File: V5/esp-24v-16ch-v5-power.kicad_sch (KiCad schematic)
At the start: 38 parts, among them J5 VIN, J6 USB_C_Receptacle_USB2.0, Q1 WPM2015-3/TR, Q2 MMUN2211LT3G, U1 SY8089A1AAC, U2 TX4138

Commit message: Created V5
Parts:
- removed F1: 33V/500mA, Tales:R_1206_3216Metric, symbol Device:Polyfuse
- added D4: USBLC6-2SC6, Package_TO_SOT_SMD:SOT-23-6, symbol Power_Protection:USBLC6-2SC6
- C3: renamed from C9; Technology Ceramix X7R -> Ceramic X7R
- J2: renamed from J6; footprint Tales:USB_C_Receptacle_GCT_USB4105-xx-A_16P_TopMnt_Horizontal -> Tales:USB_C_Receptacle_ShouHan_TYPE-C-16PLT-H10.0; LCSC Part # C2765186 -> C3151749; Mfr PN TYPE-C 16PIN 2MD(073) -> TYPE-C 16PLT-H10.0; Vendor PN C2765186 -> C3151749
- R10: renamed from R8; value 10k/62,5mW -> 10k
- R11: renamed from R9; value 1k/62,5mW -> 1k
- R5: renamed from R2; value 5,1k/62,5mW -> 5,1k
- R6: renamed from R3; value 5,1k/62,5mW -> 5,1k
- R7: renamed from R1; value 560R/100mW -> 1k; LCSC Part # C23204 -> C11702; Mfr PN 0603WAF5600T5E -> 0402WGF1002TCE; Vendor PN C23204 -> C11702
- renumbered C2 to C1, C7 to C10, C8 to C11, C11 to C12, C3 to C2, C10 to C4, C12 to C5, C5 to C6, C6 to C7, C1 to C8, C4 to C9, D2 to D1, D4 to D2, D5 to D3, D3 to D5, D1 to D6, J5 to J1, L2 to L1, L1 to L2, R6 to R1, R7 to R2, R10 to R3, R11 to R4, R4 to R8, R5 to R9, U2 to U1, U1 to U2
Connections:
- net +5V: now also D5.1 (K)
- net GND: now also D4.2 (GND)
- net 5VLED: now reaches D6.2 (A), R7.2
- net 5VSW: now reaches C3.2, D2.1 (K), L1.1, U1.1 (SW)
- net 3V3SW: now reaches L2.1, U2.3 (LX)
- net PHYPWRFET: now reaches C11.2, Q1.1 (G), R10.2, R11.2
- net 5VRC: now reaches C3.1, R2.1
- net PHYPWRBJT: now reaches Q2.3 (C), R11.1
- net ILIM: now reaches R1.2, U1.2 (ILIM), U1.9 (ILIM)
- net 5VREF: now reaches C4.2, R3.2, R4.1, U1.5 (FB)
- net +3.3V renamed +3V3
- net +3.3VA renamed +3V3A
- net +3.3VLAN renamed +3V3LAN
- net 24VIN renamed +24VIN
- net 3.3V_REF renamed 3V3REF
- net 5V_MAIN renamed 5VMAIN
- net 5V_USB renamed 5VUSB
- net 5VUSB: now also D4.5 (VBUS)
- net PHY_PWR renamed PHYPWR
- net USB_A5 renamed USBCC1
- net USB_B5 renamed USBCC2
- net USB_D+ renamed USBCD+
- net USBCD+: now also D4.3 (I/O2)
- net USB_D- renamed USBCD-
- net USBCD-: now also D4.1 (I/O1)
- new net USBD+: D4.4 (I/O2)
- new net USBD-: D4.6 (I/O1)
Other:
- note added: "I_{LED} = (5V - V_{LED}) / 1k I_{LED} = (5V - 2.7V) / 1k I_{LED} = 2,30 mA"
- title: ESP 24V 16xIn/16xOut/4xNTC Module -> ESP 24V 16xIn/16xOut/1-Wire Module
- moved on the sheet: C1, C10, C11, C12, C2, C3, C4, C5, C6, C7, C8, C9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

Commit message: Updates and corrections to SCH and PCB
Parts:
- R7: footprint Tales:R_0603_1608Metric -> Tales:R_0402_1005Metric; Case 0603/1608 -> 0402/1005; Mfr PN 0402WGF1002TCE -> 0402WGF1001TCE
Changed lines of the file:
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@@
 			)
 		)
-		(property "Footprint" "Tales:R_0603_1608Metric"
+		(property "Footprint" "Tales:R_0402_1005Metric"
 			(at 45.466 143.764 90)
 			(effects
@@
 			)
 		)
-		(property "Case" "0603/1608"
+		(property "Case" "0402/1005"
 			(at 44.45 143.51 0)
 			(effects
@@
 			)
 		)
-		(property "Mfr PN" "0402WGF1002TCE"
+		(property "Mfr PN" "0402WGF1001TCE"
 			(at 44.45 143.51 0)
 			(effects

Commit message: V5.2.0
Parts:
- added R136: 0R/250mW, Tales:R_1206_3216Metric, symbol Device:R_US
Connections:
- net at U1.7 (POK): now also R136.1
- new net ESPEN: R136.2
- no-connect marks 4 -> 3
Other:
- moved on the sheet: L2, R1

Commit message: Back to V5.1.0
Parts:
- removed R136: 0R/250mW, Tales:R_1206_3216Metric, symbol Device:R_US
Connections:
- no-connect marks 3 -> 4
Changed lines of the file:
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@@
 	)
 	(no_connect
+		(at 153.67 39.37)
+	)
+	(no_connect
 		(at 153.67 36.83)
 	)
@@
 	(wire
 		(pts
-			(xy 146.05 52.07) (xy 146.05 57.15)
-		)
-		(stroke
-			(width 0)
-			(type default)
-		)
-	)
-	(wire
-		(pts
 			(xy 166.37 111.76) (xy 166.37 121.92)
 		)
@@
 	(wire
 		(pts
-			(xy 146.05 39.37) (xy 146.05 44.45)
-		)
-		(stroke
-			(width 0)
-			(type default)
-		)
-	)
-	(wire
-		(pts
 			(xy 74.93 144.78) (xy 96.52 144.78)
 		)
@@
 	(wire
 		(pts
-			(xy 146.05 57.15) (xy 154.94 57.15)
-		)
-		(stroke
-			(width 0)
-			(type default)
-		)
-	)
-	(wire
-		(pts
 			(xy 46.99 38.1) (xy 46.99 39.37)
 		)
@@
 	(wire
 		(pts
-			(xy 153.67 39.37) (xy 146.05 39.37)
-		)
-		(stroke
-			(width 0)
-			(type default)
-		)
-	)
-	(wire
-		(pts
 			(xy 251.46 96.52) (xy 243.84 96.52)
 		)
@@
 		)
 	)
-	(hierarchical_label "ESPEN"
-		(shape output)
-		(at 154.94 57.15 0)
-		(effects
-			(font
-				(size 1.27 1.27)
-			)
-			(justify left)
-		)
-	)
 	(hierarchical_label "PHYPWR"
 		(shape input)
@@
 					(unit 1)
 				)
-			)
-		)
-	)
-	(symbol
-		(lib_id "Device:R_US")
-		(at 146.05 48.26 0)
-		(unit 1)
-		(exclude_from_sim no)
-		(in_bom yes)
-		(on_board yes)
-		(dnp no)
-		(fields_autoplaced yes)
-		(property "Reference" "R136"
-			(at 148.59 45.7199 0)
-			(effects
-				(font
-					(size 1.27 1.27)
-				)
-				(justify left)
-			)
-		)
-		(property "Value" "0R/250mW"
-			(at 148.59 48.2599 0)
-			(effects
-				(font
-					(size 1.27 1.27)
-				)
-				(justify left)
-			)
-		)
-		(property "Footprint" "Tales:R_1206_3216Metric"
-			(at 147.066 48.514 90)
-			(effects
-				(font
-					(size 1.27 1.27)
-				)
-				(hide yes)
-			)
-		)
-		(property "Datasheet" "~"
-			(at 146.05 48.26 0)
-			(effects
-				(font
-					(size 1.27 1.27)
-				)
-				(hide yes)
-			)
-		)
-		(property "Description" "Resistor, US symbol"
-			(at 146.05 48.26 0)
-			(effects
-				(font
-					(size 1.27 1.27)
-				)
-				(hide yes)
-			)
-		)
-		(property "Technology" "1%"
-			(at 148.59 48.895 0)
-			(effects
-				(font
-					(size 1.27 1.27)
-				)
-				(justify left)
-				(hide yes)
-			)
-		)
-		(property "Mfr" "Uniroyal"
-			(at 146.05 48.26 0)
-			(effects
-				(font
-					(size 1.27 1.27)
-				)
-				(hide yes)
-			)
-		)
-		(property "Mfr PN" "1206W4F0000T5E"
-			(at 146.05 48.26 0)
-			(effects
-				(font
-					(size 1.27 1.27)
-				)
-				(hide yes)
-			)
-		)
-		(property "Vendor" "JLCPCB"
-			(at 146.05 48.26 0)
-			(effects
-				(font
-					(size 1.27 1.27)
-				)
-				(hide yes)
-			)
-		)
-		(property "Vendor PN" "C17888"
-			(at 146.05 48.26 0)
-			(effects
-				(font
-					(size 1.27 1.27)
-				)
-				(hide yes)
-			)
-		)
-		(property "LCSC Part #" "C17888"
-			(at 148.59 50.7999 0)
-			(effects
-				(font
-					(size 1.27 1.27)
-				)
-				(justify left)
-			)
-		)
-		(property "JLCPCB BOM" "1"
-			(at 146.05 48.26 0)
-			(effects
-				(font
-					(size 1.27 1.27)
-				)
-				(hide yes)
-			)
-		)
-		(property "Package" "1206/3216"
-			(at 146.05 48.26 0)
-			(effects
-				(font
-					(size 1.27 1.27)
-				)
-				(hide yes)
-			)
-		)
-		(property "Case" "1206/3216"
-			(at 146.05 48.26 0)
-			(effects
-				(font
-					(size 1.27 1.27)
-				)
-				(hide yes)
-			)
-		)
-		(pin "1"
-		)
-		(pin "2"
-		)
-		(instances
-			(project "esp-24v-16ch-v5"
-				(path "/2bc5a21a-1d79-419d-a592-6852cc07b00a/7b388c9c-6faf-4681-b727-510de2ea001e"
-					(reference "R136")
-					(unit 1)
-				)

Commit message: Many changes!
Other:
- note added: "RESISTORS: 62,5mW WHERE NOT SPECIFIED"
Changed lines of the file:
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@@
 		(rev "V5.1")
+	)
+	(text "RESISTORS: 62,5mW WHERE NOT SPECIFIED"
+		(exclude_from_sim no)
+		(at 182.88 172.72 0)
+		(effects
+			(font
+				(size 1.905 1.905)
+			)
+			(justify left)
+		)
 	)
 	(text "R_{H} = (V_{OUT} - 0,6V) * R_{L} / 0,6V\n\nV_{OUT} = (0,6 * R_{H} / R_{L}) + 0,6\nV_{OUT} = (0,6 * 100k/22,1k) +0,6\nV_{OUT} = 3,31V"

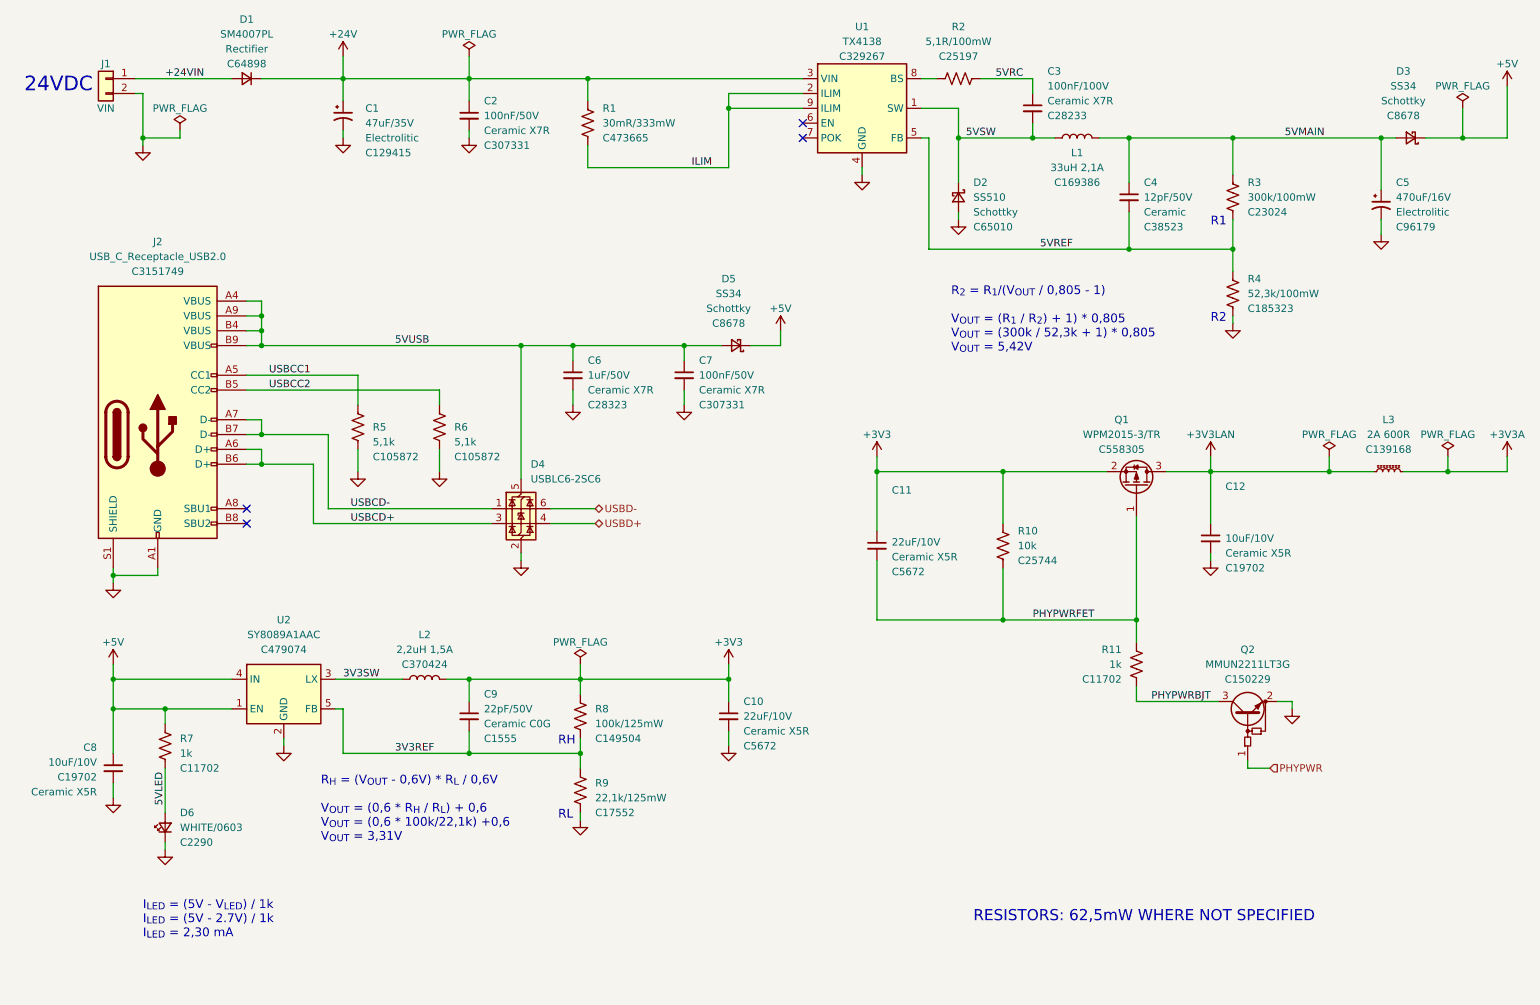
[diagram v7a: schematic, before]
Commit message: Reviewed capacitor sizes and voltages.
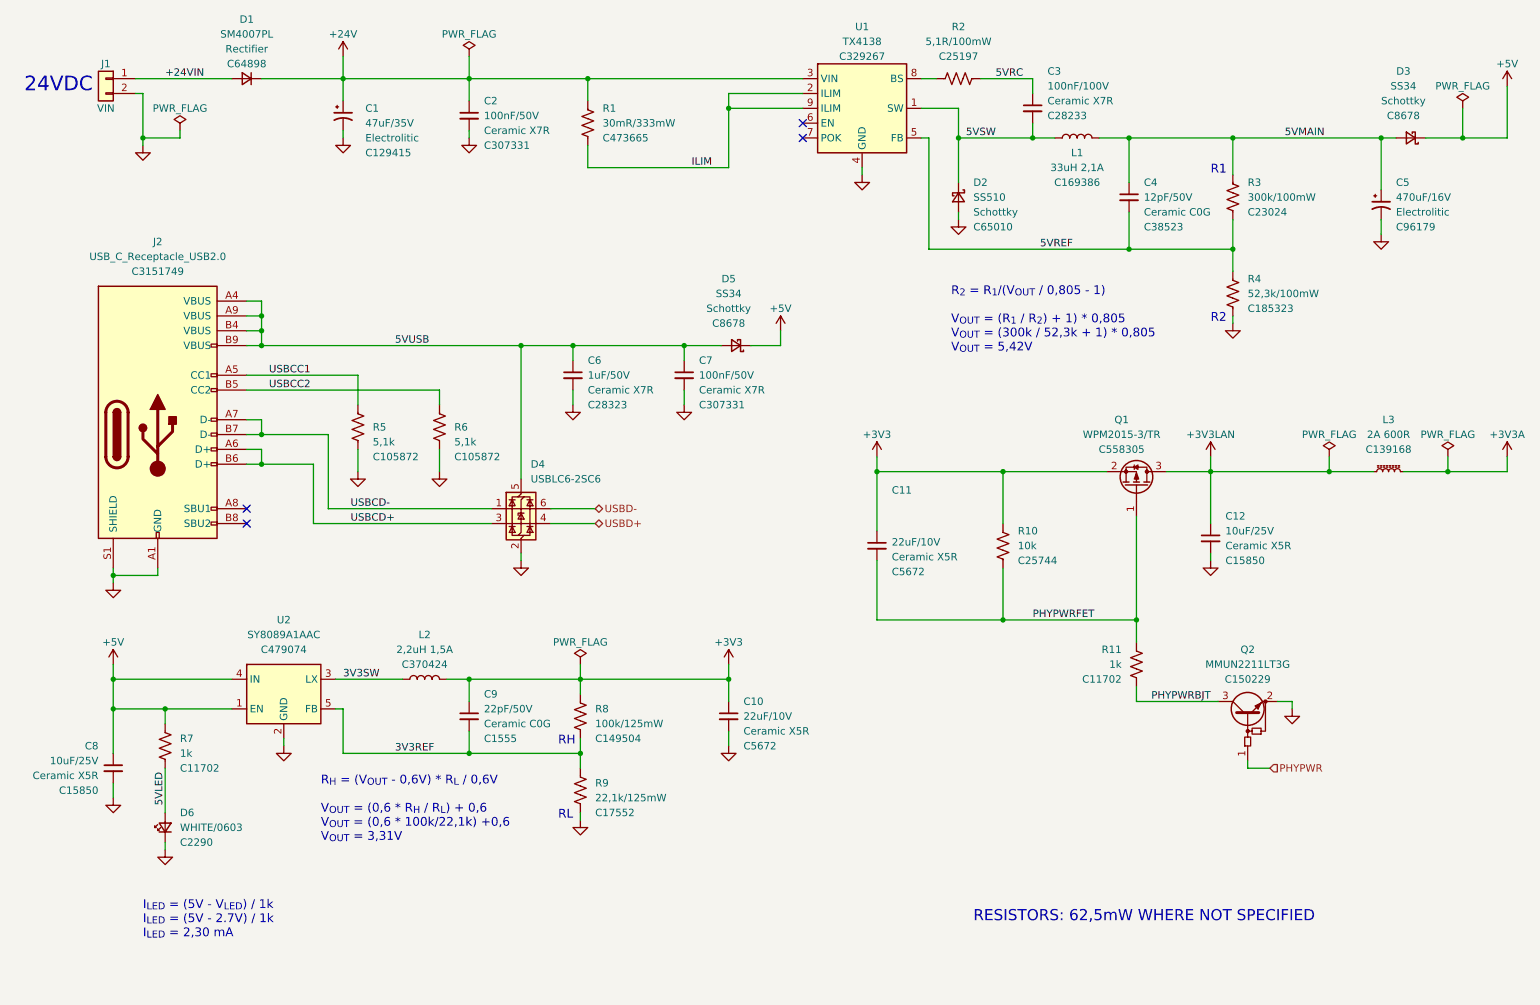
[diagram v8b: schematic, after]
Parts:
- C10, C11, R1: Package 1206/3216 -> (none)
- C12: value 10uF/10V -> 10uF/25V; footprint Tales:C_0603_1608Metric -> Tales:C_0805_2012Metric; Case 0603/1608 -> 0805/2012; LCSC Part # C19702 -> C15850; Mfr PN CL10A106KP8NNNC -> CL21A106KAYNNNE; Vendor PN C19702 -> C15850
- C2, C6, C7, C9, R10, R5, R6: Package 0402/1005 -> (none)
- C3: Package 0805/2012 -> (none)
- C4: Technology Ceramic -> Ceramic C0G
- C5: Package D8xL10.5mm -> (none)
- C8: value 10uF/10V -> 10uF/25V; footprint Tales:C_0603_1608Metric -> Tales:C_0805_2012Metric; Case 0603/1608 -> 0805/2012; LCSC Part # C19702 -> C15850; Mfr PN CL10A106KP8NNNC -> CL21A106KAYNNNE; Package 0603/1608 -> (none); Vendor PN C19702 -> C15850
- R2, R3, R4: Package 0603/1608 -> (none)
